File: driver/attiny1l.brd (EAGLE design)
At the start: 35.8 x 20 mm, 7 parts, among them IC1 ATTiny85, IC2 74AHC1G00DCK, IC3 74AHC1G00DCK, IC4 LB1973M, J1 AVR_SPI_PRG_6NS

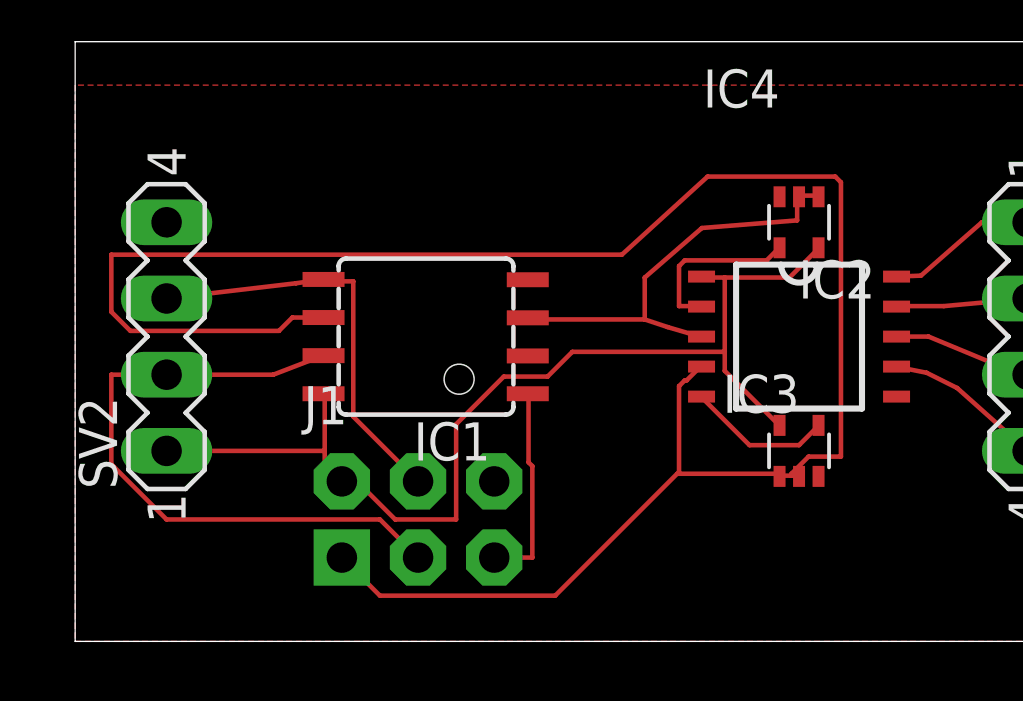
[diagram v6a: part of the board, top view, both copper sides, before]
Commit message: adjust routing for easier soldering withoud soldermask
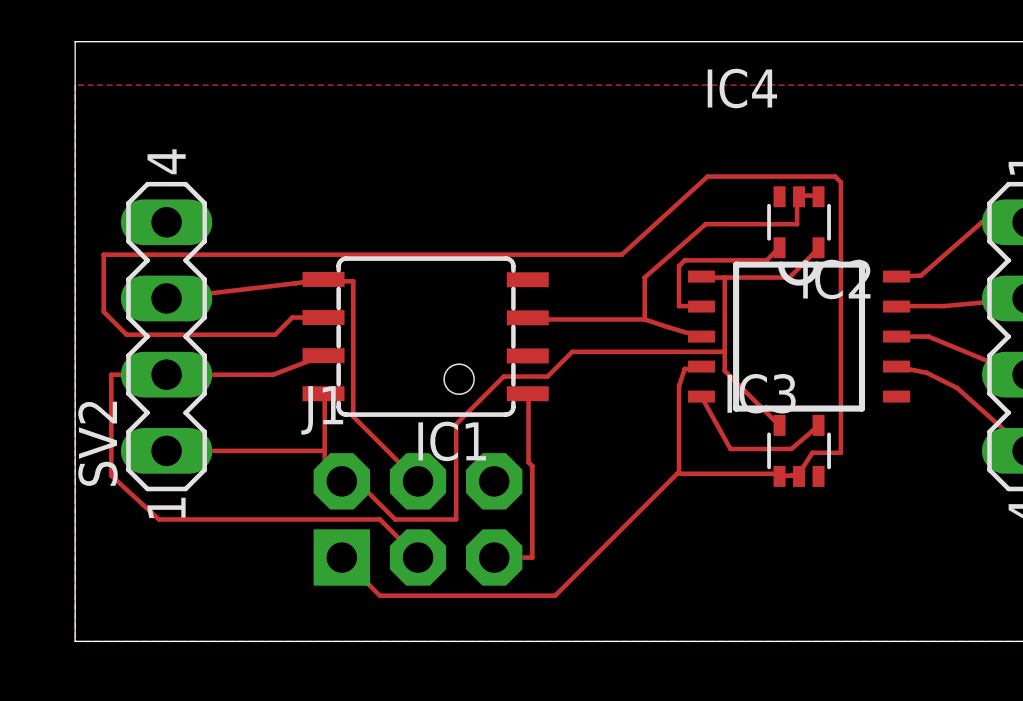
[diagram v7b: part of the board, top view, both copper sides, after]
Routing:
- net IN1/MISO: track 67.5 -> 68.2 mm
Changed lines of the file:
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@@
 <setting verticaltext="up"/>
 </settings>
-<grid distance="10" unitdist="mil" unit="mm" style="lines" multiple="1" display="yes" altdistance="5" altunitdist="mm" altunit="mm"/>
+<grid distance="5" unitdist="mil" unit="mil" style="lines" multiple="1" display="yes" altdistance="5" altunitdist="mm" altunit="mm"/>
 <layers>
 <layer number="1" name="Top" color="4" fill="1" visible="yes" active="yes"/>
@@
 <contactref element="IC3" pad="4"/>
 <contactref element="IC4" pad="5"/>
-<wire x1="24.13" y1="6.5405" x2="24.765" y2="7.1755" width="0.1524" layer="1"/>
-<wire x1="22.479" y1="6.5405" x2="24.13" y2="6.5405" width="0.1524" layer="1"/>
-<wire x1="20.8915" y1="8.128" x2="22.479" y2="6.5405" width="0.1524" layer="1"/>
+<wire x1="23.876" y1="6.4135" x2="24.765" y2="7.1755" width="0.1524" layer="1"/>
+<wire x1="21.844" y1="6.4135" x2="23.876" y2="6.4135" width="0.1524" layer="1"/>
+<wire x1="20.8915" y1="8.128" x2="21.844" y2="6.4135" width="0.1524" layer="1"/>
 <wire x1="24.765" y1="7.1755" x2="24.78" y2="7.2" width="0.1524" layer="1"/>
 <wire x1="20.8915" y1="8.128" x2="20.88" y2="8.16" width="0.1524" layer="1"/>
@@
 <wire x1="23.495" y1="5.5245" x2="23.48" y2="5.5" width="0.1524" layer="1"/>
 <wire x1="24.13" y1="5.5245" x2="24.13" y2="5.5" width="0.1524" layer="1"/>
-<wire x1="20.3835" y1="8.6995" x2="20.828" y2="9.144" width="0.1524" layer="1"/>
-<wire x1="20.32" y1="8.6995" x2="20.3835" y2="8.6995" width="0.1524" layer="1"/>
-<wire x1="20.1295" y1="8.509" x2="20.32" y2="8.6995" width="0.1524" layer="1"/>
+<wire x1="20.6375" y1="9.0805" x2="20.828" y2="9.144" width="0.1524" layer="1"/>
+<wire x1="20.32" y1="9.0805" x2="20.6375" y2="9.0805" width="0.1524" layer="1"/>
+<wire x1="20.1295" y1="8.509" x2="20.32" y2="9.0805" width="0.1524" layer="1"/>
 <wire x1="20.1295" y1="5.588" x2="20.1295" y2="8.509" width="0.1524" layer="1"/>
 <wire x1="23.495" y1="5.588" x2="20.1295" y2="5.588" width="0.1524" layer="1"/>
 <wire x1="20.828" y1="9.144" x2="20.88" y2="9.16" width="0.1524" layer="1"/>
 <wire x1="23.495" y1="5.588" x2="23.48" y2="5.5" width="0.1524" layer="1"/>
-<wire x1="6.7945" y1="10.3505" x2="7.239" y2="10.795" width="0.1524" layer="1"/>
-<wire x1="1.8415" y1="10.3505" x2="6.7945" y2="10.3505" width="0.1524" layer="1"/>
-<wire x1="1.2065" y1="10.9855" x2="1.8415" y2="10.3505" width="0.1524" layer="1"/>
-<wire x1="1.2065" y1="12.8905" x2="1.2065" y2="10.9855" width="0.1524" layer="1"/>
-<wire x1="18.2245" y1="12.8905" x2="1.2065" y2="12.8905" width="0.1524" layer="1"/>
+<wire x1="6.6675" y1="10.2235" x2="7.239" y2="10.795" width="0.1524" layer="1"/>
+<wire x1="1.7145" y1="10.2235" x2="6.6675" y2="10.2235" width="0.1524" layer="1"/>
+<wire x1="0.9525" y1="10.9855" x2="1.7145" y2="10.2235" width="0.1524" layer="1"/>
+<wire x1="0.9525" y1="12.8905" x2="0.9525" y2="10.9855" width="0.1524" layer="1"/>
+<wire x1="18.2245" y1="12.8905" x2="0.9525" y2="12.8905" width="0.1524" layer="1"/>
 <wire x1="21.082" y1="15.494" x2="18.2245" y2="12.8905" width="0.1524" layer="1"/>
 <wire x1="25.3365" y1="15.494" x2="21.082" y2="15.494" width="0.1524" layer="1"/>
 <wire x1="25.527" y1="15.3035" x2="25.3365" y2="15.494" width="0.1524" layer="1"/>
-<wire x1="25.527" y1="6.1595" x2="25.527" y2="15.3035" width="0.1524" layer="1"/>
-<wire x1="24.4475" y1="6.1595" x2="25.527" y2="6.1595" width="0.1524" layer="1"/>
-<wire x1="23.876" y1="5.588" x2="24.4475" y2="6.1595" width="0.1524" layer="1"/>
+<wire x1="25.527" y1="6.2865" x2="25.527" y2="15.3035" width="0.1524" layer="1"/>
+<wire x1="24.5745" y1="6.2865" x2="25.527" y2="6.2865" width="0.1524" layer="1"/>
+<wire x1="24.13" y1="5.588" x2="24.5745" y2="6.2865" width="0.1524" layer="1"/>
 <wire x1="7.239" y1="10.795" x2="8.28" y2="10.795" width="0.1524" layer="1"/>
-<wire x1="23.876" y1="5.588" x2="23.876" y2="5.5245" width="0.1524" layer="1"/>
+<wire x1="24.13" y1="5.588" x2="23.876" y2="5.5245" width="0.1524" layer="1"/>
 <wire x1="10.16" y1="1.524" x2="8.89" y2="2.794" width="0.1524" layer="1"/>
 <wire x1="16.002" y1="1.524" x2="10.16" y2="1.524" width="0.1524" layer="1"/>
@@
 <wire x1="20.828" y1="10.16" x2="20.88" y2="10.16" width="0.1524" layer="1"/>
 <wire x1="15.113" y1="10.7315" x2="15.088" y2="10.785" width="0.1524" layer="1"/>
-<wire x1="24.0665" y1="14.0335" x2="24.0665" y2="14.7955" width="0.1524" layer="1"/>
-<wire x1="20.8915" y1="13.7795" x2="24.0665" y2="14.0335" width="0.1524" layer="1"/>
-<wire x1="18.9865" y1="12.1285" x2="20.8915" y2="13.7795" width="0.1524" layer="1"/>
+<wire x1="24.0665" y1="13.9065" x2="24.0665" y2="14.7955" width="0.1524" layer="1"/>
+<wire x1="21.0185" y1="13.9065" x2="24.0665" y2="13.9065" width="0.1524" layer="1"/>
+<wire x1="18.9865" y1="12.1285" x2="21.0185" y2="13.9065" width="0.1524" layer="1"/>
 <wire x1="18.9865" y1="10.7315" x2="18.9865" y2="12.1285" width="0.1524" layer="1"/>
 <wire x1="24.0665" y1="14.7955" x2="24.13" y2="14.82" width="0.1524" layer="1"/>
@@
 <vertex x="35.814" y="18.542"/>
 </polygon>
+<wire x1="23.48" y1="14.82" x2="27.38" y2="8.16" width="0" layer="19" extent="1-1"/>
 <wire x1="13.97" y1="5.334" x2="15.088" y2="12.055" width="0" layer="19" extent="1-1"/>
-<wire x1="27.38" y1="8.16" x2="23.48" y2="14.82" width="0" layer="19" extent="1-1"/>
 </signal>
 <signal name="+5V">
@@
 <wire x1="8.255" y1="9.525" x2="8.28" y2="9.525" width="0.1524" layer="1"/>
 <wire x1="10.16" y1="4.064" x2="11.43" y2="2.794" width="0.1524" layer="1"/>
-<wire x1="3.048" y1="4.064" x2="10.16" y2="4.064" width="0.1524" layer="1"/>
-<wire x1="1.2065" y1="5.9055" x2="3.048" y2="4.064" width="0.1524" layer="1"/>
-<wire x1="1.2065" y1="8.89" x2="1.2065" y2="5.9055" width="0.1524" layer="1"/>
+<wire x1="2.794" y1="4.064" x2="10.16" y2="4.064" width="0.1524" layer="1"/>
+<wire x1="1.2065" y1="5.5245" x2="2.794" y2="4.064" width="0.1524" layer="1"/>
+<wire x1="1.2065" y1="8.89" x2="1.2065" y2="5.5245" width="0.1524" layer="1"/>
 <wire x1="3.048" y1="8.89" x2="1.2065" y2="8.89" width="0.1524" layer="1"/>
 </signal>

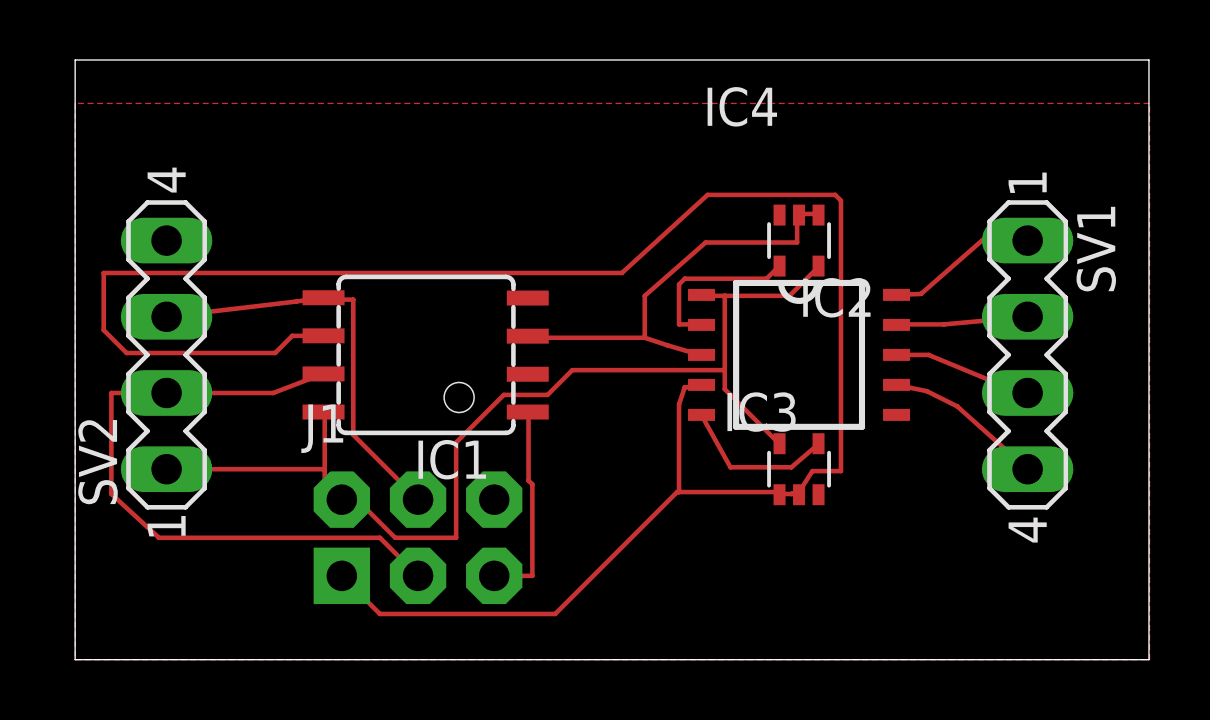
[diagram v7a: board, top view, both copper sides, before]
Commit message: it seems this still works with 8mil trace width
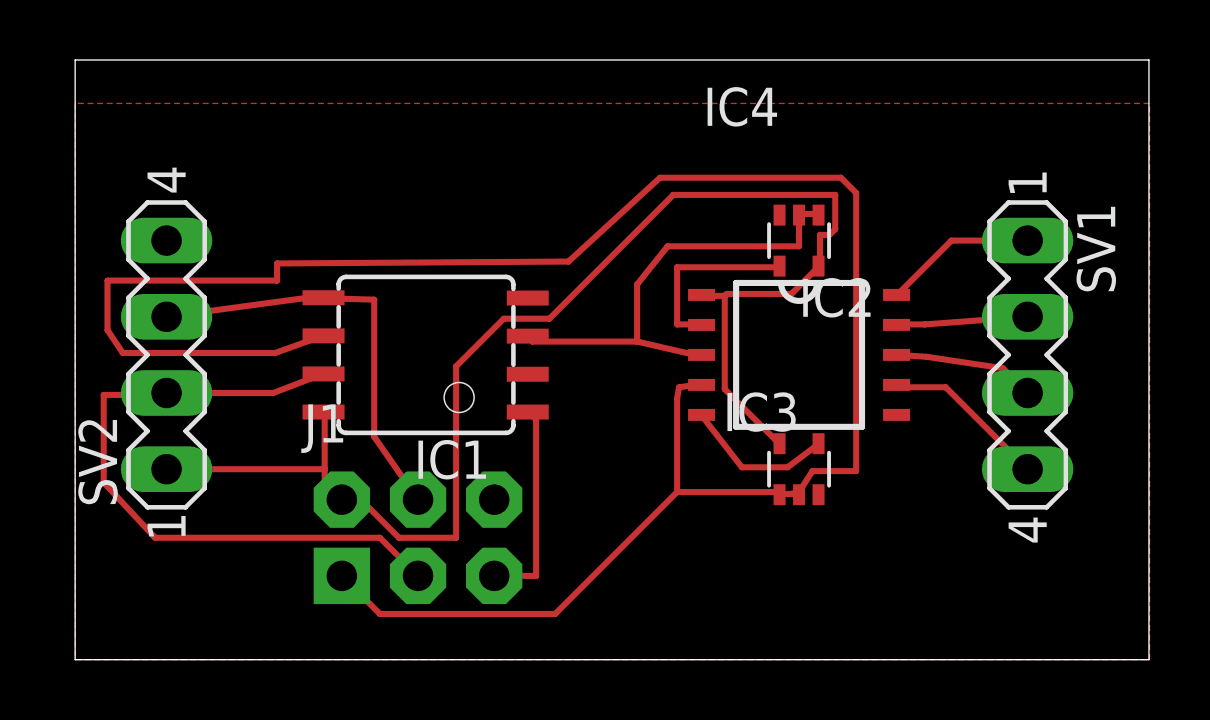
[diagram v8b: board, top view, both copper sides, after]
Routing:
- net +5V: track 36.3 -> 46.7 mm
- net IN1/MISO: track 68.2 -> 69.8 mm
- net IN3: track 14.7 -> 15.6 mm
- net SDA/MOSI: track 13.9 -> 14.6 mm
